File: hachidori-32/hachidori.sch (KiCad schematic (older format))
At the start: 42 parts, among them P1 VIN, P2 UART, P4 I2C, SW1 FLASH, SW2 RESET, U1 NCP1117ST33, U2 MPU-9250, U4 BME280, U7 INA226

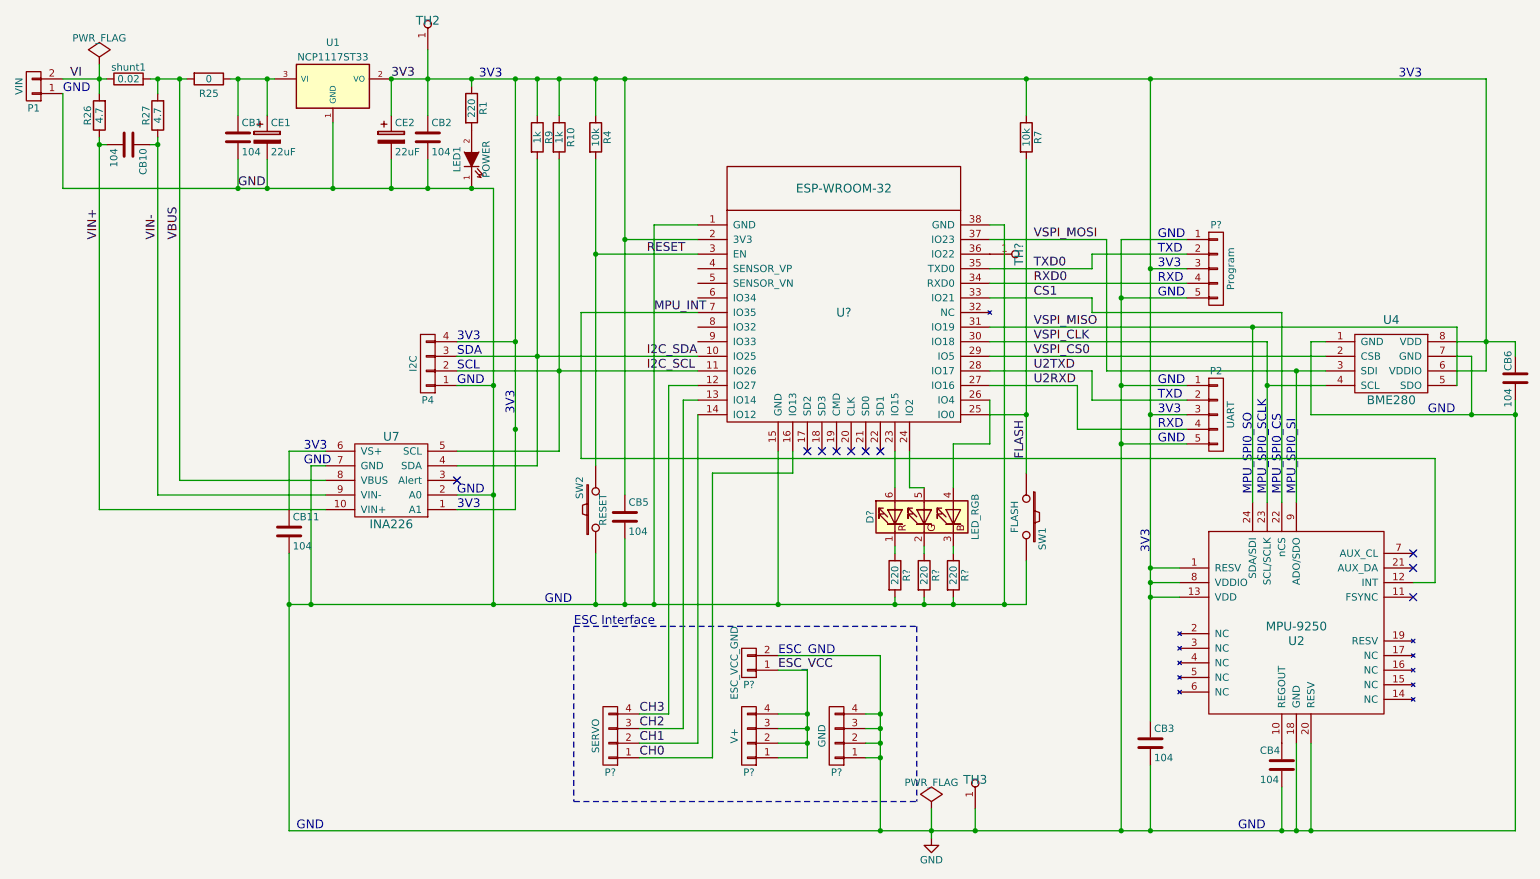
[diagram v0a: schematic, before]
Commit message: Fix I2C and GPIO pin header
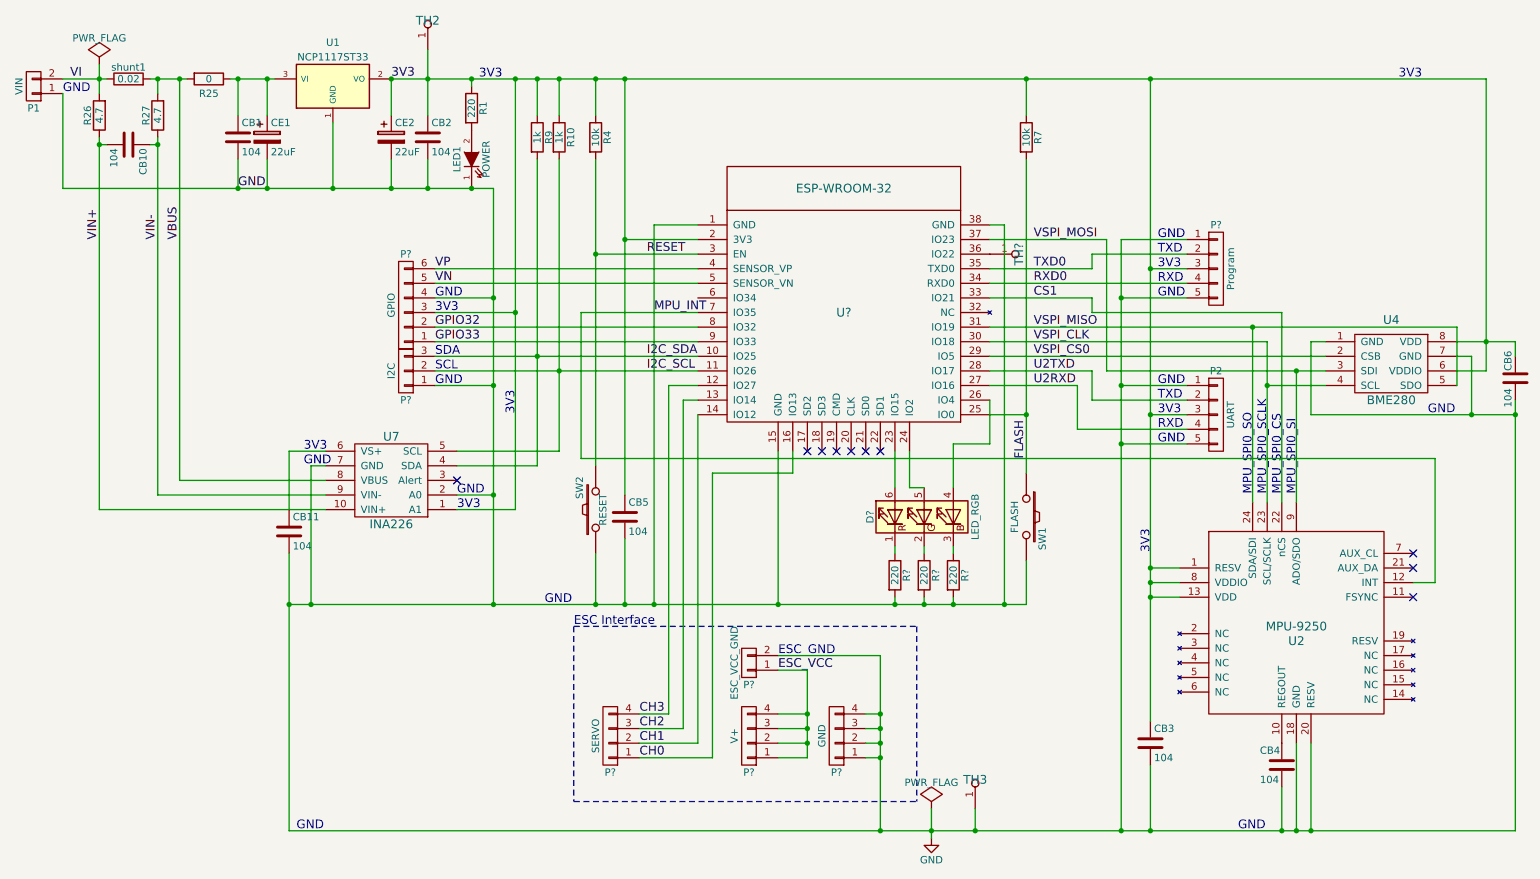
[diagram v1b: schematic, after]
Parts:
- removed P4: I2C, droneworks:Pin_Header_1x04, symbol CONN_01X04
- added P?: I2C, symbol CONN_01X03
- added P?: GPIO, symbol CONN_01X06
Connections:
- net 3V3: now also P?.3 (P3)
- net GND: now also P?.1 (P1), P?.4 (P4)
- net I2C_SCL: now also P?.2 (P2)
- net I2C_SDA: now also P?.3 (P3)
- net VP: now reaches U?.4 (SENSOR_VP)
- net VP: now also P?.6 (P6)
- net VN: now reaches U?.5 (SENSOR_VN)
- net VN: now also P?.5 (P5)
- net GPIO32: now reaches U?.8 (IO32)
- net GPIO32: now also P?.2 (P2)
- net GPIO33: now reaches U?.9 (IO33)
- net GPIO33: now also P?.1 (P1)

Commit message: Change Regulator and Shunt resistor
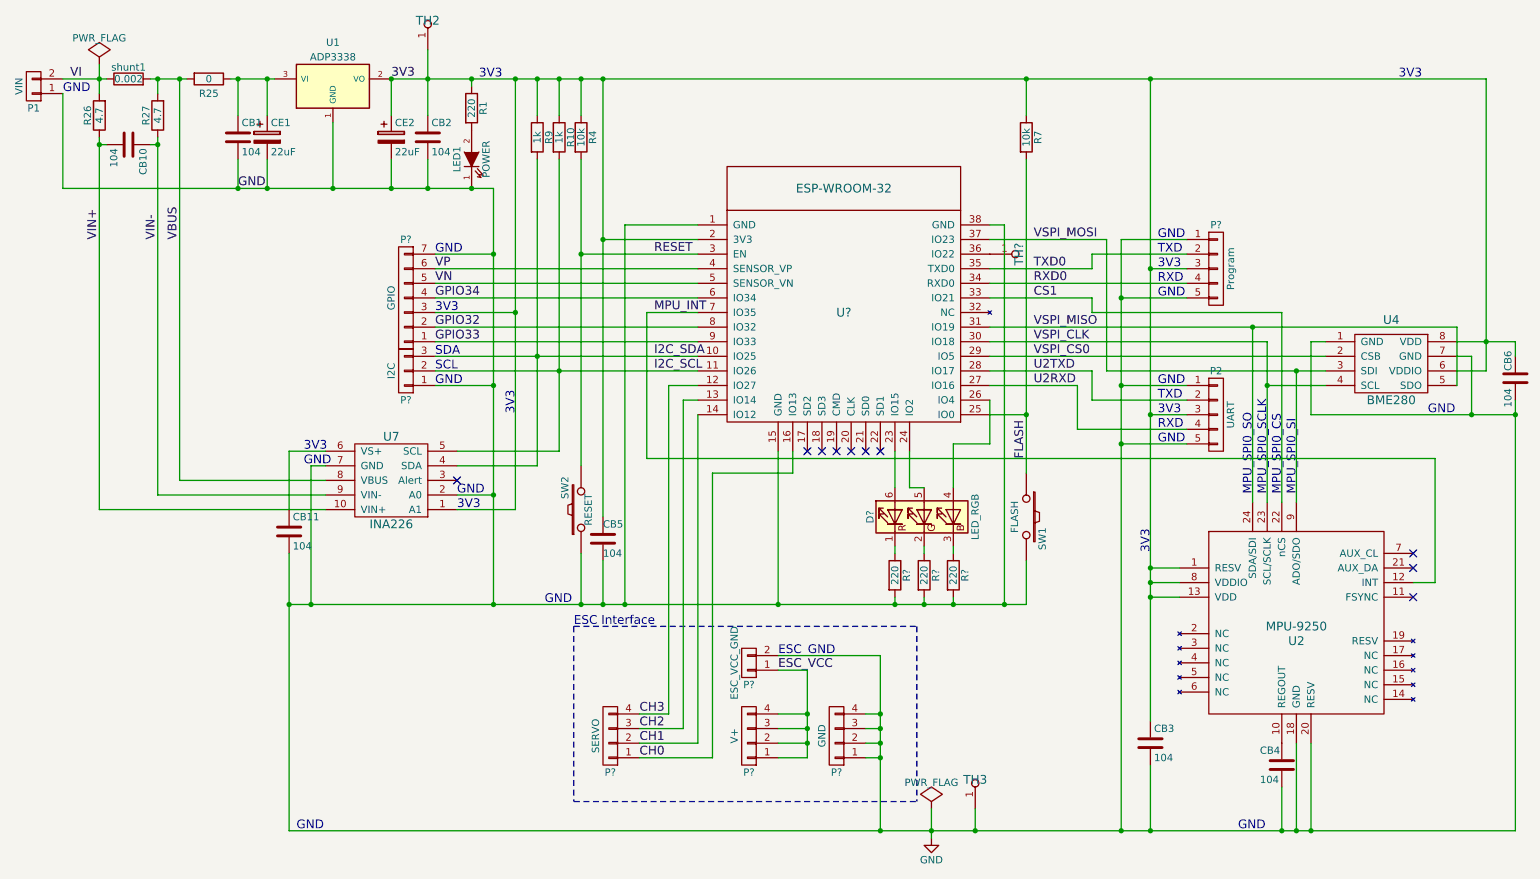
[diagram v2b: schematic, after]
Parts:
- removed P?: GPIO, symbol CONN_01X06
- added P?: GPIO, symbol CONN_01X07
- U1: value NCP1117ST33 -> ADP3338
- shunt1: value 0.02 -> 0.002
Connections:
- net 3V3: now also P?.3 (P3)
- net GND: now also P?.7 (P7); no longer R7.2, SW1.1, U2.12 (INT), U?.25 (IO0), U?.7 (IO35)
- net GPIO32: now also P?.2 (P2)
- net GPIO33: now also P?.1 (P1)
- net VN: now also P?.5 (P5)
- net VP: now also P?.6 (P6)
- net GPIO34: now reaches U?.6 (IO34)
- net GPIO34: now also P?.4 (P4)
- new net FLASH: R7.2, SW1.1, U2.12 (INT), U?.25 (IO0), U?.7 (IO35)
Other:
- moved on the sheet: CB5, R4, SW2
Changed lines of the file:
@@
 Title "hachidori-32"
 Date "2017-02-15"
-Rev "0.06"
+Rev "0.07"
 Comp ""
 Comment1 "Copyright (c) 2016 DroneWorks Inc."
@@
 L R R4
 U 1 1 57B2B6BF
-P 4550 1750
-F 0 "R4" V 4630 1750 50  0000 C CNN
-F 1 "10k" V 4550 1750 50  0000 C CNN
-F 2 "rohm:MCR03" V 4480 1750 50  0001 C CNN
-F 3 "" H 4550 1750 50  0000 C CNN
-	1    4550 1750
+P 4450 1750
+F 0 "R4" V 4530 1750 50  0000 C CNN
+F 1 "10k" V 4450 1750 50  0000 C CNN
+F 2 "rohm:MCR03" V 4380 1750 50  0001 C CNN
+F 3 "" H 4450 1750 50  0000 C CNN
+	1    4450 1750
 	1    0    0    -1
 $EndComp
@@
 L C CB5
 U 1 1 57B2DF30
-P 4750 4350
-F 0 "CB5" H 4775 4450 50  0000 L CNN
-F 1 "104" H 4775 4250 50  0000 L CNN
-F 2 "droneworks:GRM18" H 4788 4200 50  0001 C CNN
-F 3 "" H 4750 4350 50  0000 C CNN
-	1    4750 4350
+P 4600 4500
+F 0 "CB5" H 4600 4600 50  0000 L CNN
+F 1 "104" H 4600 4400 50  0000 L CNN
+F 2 "droneworks:GRM18" H 4638 4350 50  0001 C CNN
+F 3 "" H 4600 4500 50  0000 C CNN
+	1    4600 4500
 	1    0    0    -1
 $EndComp
@@
 P 2750 1400
 F 0 "U1" H 2750 1700 50  0000 C CNN
-F 1 "NCP1117ST33" H 2750 1600 50  0000 C CNN
+F 1 "ADP3338" H 2750 1600 50  0000 C CNN
 F 2 "droneworks:NCP1117ST" H 2750 1400 50  0001 C CNN
 F 3 "" H 2750 1400 50  0000 C CNN
@@
 Text Label 2100 2100 0    60   ~ 0
 GND
-Text Label 4900 3250 0    60   ~ 0
+Text Label 4950 3250 0    60   ~ 0
 I2C_SDA
-Text Label 4900 3350 0    60   ~ 0
+Text Label 4950 3350 0    60   ~ 0
 I2C_SCL
 Text Notes 2500 6500 0    60   ~ 0
@@
 L SW_PUSH SW2
 U 1 1 57BDEBB2
-P 4550 4300
-F 0 "SW2" H 4700 4410 50  0000 C CNN
-F 1 "RESET" H 4550 4250 50  0000 C CNN
-F 2 "droneworks:B3U-1000P" H 4550 4300 50  0001 C CNN
-F 3 "" H 4550 4300 50  0000 C CNN
-	1    4550 4300
+P 4450 4300
+F 0 "SW2" H 4600 4410 50  0000 C CNN
+F 1 "RESET" H 4450 4250 50  0000 C CNN
+F 2 "droneworks:B3U-1000P" H 4450 4300 50  0001 C CNN
+F 3 "" H 4450 4300 50  0000 C CNN
+	1    4450 4300
 	0    -1   -1   0
 $EndComp
@@
 P 1350 1350
 F 0 "shunt1" V 1430 1350 50  0000 C CNN
-F 1 "0.02" V 1350 1350 50  0000 C CNN
+F 1 "0.002" V 1350 1350 50  0000 C CNN
 F 2 "rohm:MCR03" V 1280 1350 50  0001 C CNN
 F 3 "" H 1350 1350 50  0000 C CNN
@@
 Text Notes 9350 4200 1    60   ~ 0
 MPU_SPI0_SI
-Text Label 4900 2550 0    60   ~ 0
+Text Label 4950 2550 0    60   ~ 0
 RESET
 Text Notes 8350 4600 1    60   ~ 0
@@
 Wire Wire Line
 	3700 2100 3850 2100
-Connection ~ 4550 2550
+Connection ~ 4450 2550
 Connection ~ 9450 6500
 Wire Wire Line
@@
 Wire Wire Line
 	8350 4900 8350 5750
-Connection ~ 4750 4950
-Wire Wire Line
-	4750 4950 4750 4500
+Connection ~ 4600 4950
+Wire Wire Line
+	4600 4950 4600 4650
 Wire Wire Line
 	3700 1700 3700 1700
@@
 	4150 1350 4300 1350
 Wire Wire Line
-	4300 1350 4550 1350
-Wire Wire Line
-	4550 1350 4750 1350
-Wire Wire Line
-	4750 1350 7500 1350
+	4300 1350 4450 1350
+Wire Wire Line
+	4450 1350 4600 1350
+Wire Wire Line
+	4600 1350 7500 1350
 Wire Wire Line
 	7500 1350 8350 1350
@@
 	8350 1350 10650 1350
 Wire Wire Line
-	4750 2450 5250 2450
+	4600 2450 5250 2450
 Wire Wire Line
 	900  1350 1150 1350
@@
 Connection ~ 2750 2100
 Connection ~ 8350 4900
-Connection ~ 4750 2450
+Connection ~ 4600 2450
 Connection ~ 8350 4700
 Connection ~ 8350 4800
@@
 	8350 4700 8550 4700
 Wire Wire Line
-	4750 1350 4750 2450
-Wire Wire Line
-	4750 2450 4750 4200
+	4600 1350 4600 2450
+Wire Wire Line
+	4600 2450 4600 4350
 Wire Wire Line
 	2750 1650 2750 2100
@@
 Connection ~ 10550 3650
 Wire Wire Line
-	4550 2550 5250 2550
+	4450 2550 5250 2550
 Wire Wire Line
 	2450 6500 6500 6500
@@
 	2600 4950 3850 4950
 Wire Wire Line
-	3850 4950 4550 4950
-Wire Wire Line
-	4550 4950 4750 4950
-Wire Wire Line
-	4750 4950 4950 4950
-Wire Wire Line
-	4950 4950 5800 4950
+	3850 4950 4450 4950
+Wire Wire Line
+	4450 4950 4600 4950
+Wire Wire Line
+	4600 4950 4750 4950
+Wire Wire Line
+	4750 4950 5800 4950
 Wire Wire Line
 	5800 4950 6600 4950
@@
 	1700 1350 1700 4100
 Wire Wire Line
-	3850 2100 3850 2850
-Wire Wire Line
-	3850 2850 3850 3450
+	3850 2100 3850 2550
+Wire Wire Line
+	3850 2550 3850 3450
 Wire Wire Line
 	3850 3450 3850 4200
@@
 	4300 1350 4300 1600
 Wire Wire Line
-	4550 1900 4550 2550
-Wire Wire Line
-	4550 2550 4550 4000
+	4450 1900 4450 2550
+Wire Wire Line
+	4450 2550 4450 4000
 Wire Wire Line
 	6500 5300 6500 5700
@@
 Connection ~ 7500 3650
 Wire Wire Line
-	4950 2350 5250 2350
-Wire Wire Line
-	4950 4950 4950 2350
+	4750 2350 5250 2350
+Wire Wire Line
+	4750 4950 4750 2350
 Wire Wire Line
 	7250 3150 9150 3150
@@
 	1550 1450 1550 1350
 Wire Wire Line
-	4550 1350 4550 1600
+	4450 1350 4450 1600
 Connection ~ 4300 1350
-Connection ~ 4550 1350
+Connection ~ 4450 1350
 Wire Wire Line
 	7500 1350 7500 1600
-Connection ~ 4750 1350
+Connection ~ 4600 1350
 Connection ~ 7500 1350
 Wire Wire Line
@@
 	5800 5300 6500 5300
 Wire Wire Line
-	4550 4950 4550 4600
-Connection ~ 4550 4950
+	4450 4950 4450 4600
+Connection ~ 4450 4950
 Wire Notes Line
 	4400 5100 6750 5100
@@
 Wire Wire Line
 	5800 4950 5800 3900
-Connection ~ 4950 4950
+Connection ~ 4750 4950
 Wire Wire Line
 	8050 3350 8050 2450
@@
 Connection ~ 8150 3450
 Wire Wire Line
-	4450 2950 5250 2950
-Wire Wire Line
 	3850 3450 3450 3450
 Wire Wire Line
@@
 	9450 3150 9450 3650
 Wire Wire Line
-	4450 2950 4450 3950
-Wire Wire Line
-	4450 3950 10300 3950
+	4900 3950 10300 3950
 Wire Wire Line
 	10300 3950 10300 4800
@@
 	5250 2750 3450 2750
 Wire Wire Line
-	3850 2850 3450 2850
-Connection ~ 3850 2850
-Wire Wire Line
 	5250 2650 3450 2650
-Text Notes 3450 2850 0    60   ~ 0
+Text Notes 3450 2550 0    60   ~ 0
 GND
 $Comp
@@
 	-1   0    0    1
 $EndComp
-$Comp
-L CONN_01X06 P?
-U 1 1 58A45135
-P 3250 2900
-F 0 "P?" H 3250 2550 50  0000 C CNN
-F 1 "GPIO" V 3350 2900 50  0000 C CNN
-F 2 "" H 3250 2900 50  0000 C CNN
-F 3 "" H 3250 2900 50  0000 C CNN
-	1    3250 2900
-	-1   0    0    1
-$EndComp
 Text Label 3450 2650 0    60   ~ 0
 VP
@@
 Text Label 3450 3150 0    60   ~ 0
 GPIO33
+Wire Wire Line
+	3450 2850 5250 2850
+Text Label 3450 2850 0    60   ~ 0
+GPIO34
+$Comp
+L CONN_01X07 P?
+U 1 1 58A47991
+P 3250 2850
+F 0 "P?" H 3250 2450 50  0000 C CNN
+F 1 "GPIO" V 3350 2850 50  0000 C CNN
+F 2 "" H 3250 2850 50  0000 C CNN
+F 3 "" H 3250 2850 50  0000 C CNN
+	1    3250 2850
+	-1   0    0    1
+$EndComp
+Wire Wire Line
+	3450 2550 3850 2550
+Connection ~ 3850 2550
+Wire Wire Line
+	4900 3950 4900 2950
+Wire Wire Line
+	4900 2950 5250 2950
 $EndSCHEMATC
